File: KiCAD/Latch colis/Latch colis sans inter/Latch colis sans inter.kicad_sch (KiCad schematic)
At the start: 12 parts, among them J1 KF301-2P, J2 KF301-2P, J3 KF301-2P, J4 Jauges, K1 Relay_SPDT, K2 Relay_SPDT, Q1 2N2222A, U1 Heltec_LoRa32_V2_RST_side, U2 Module HX711

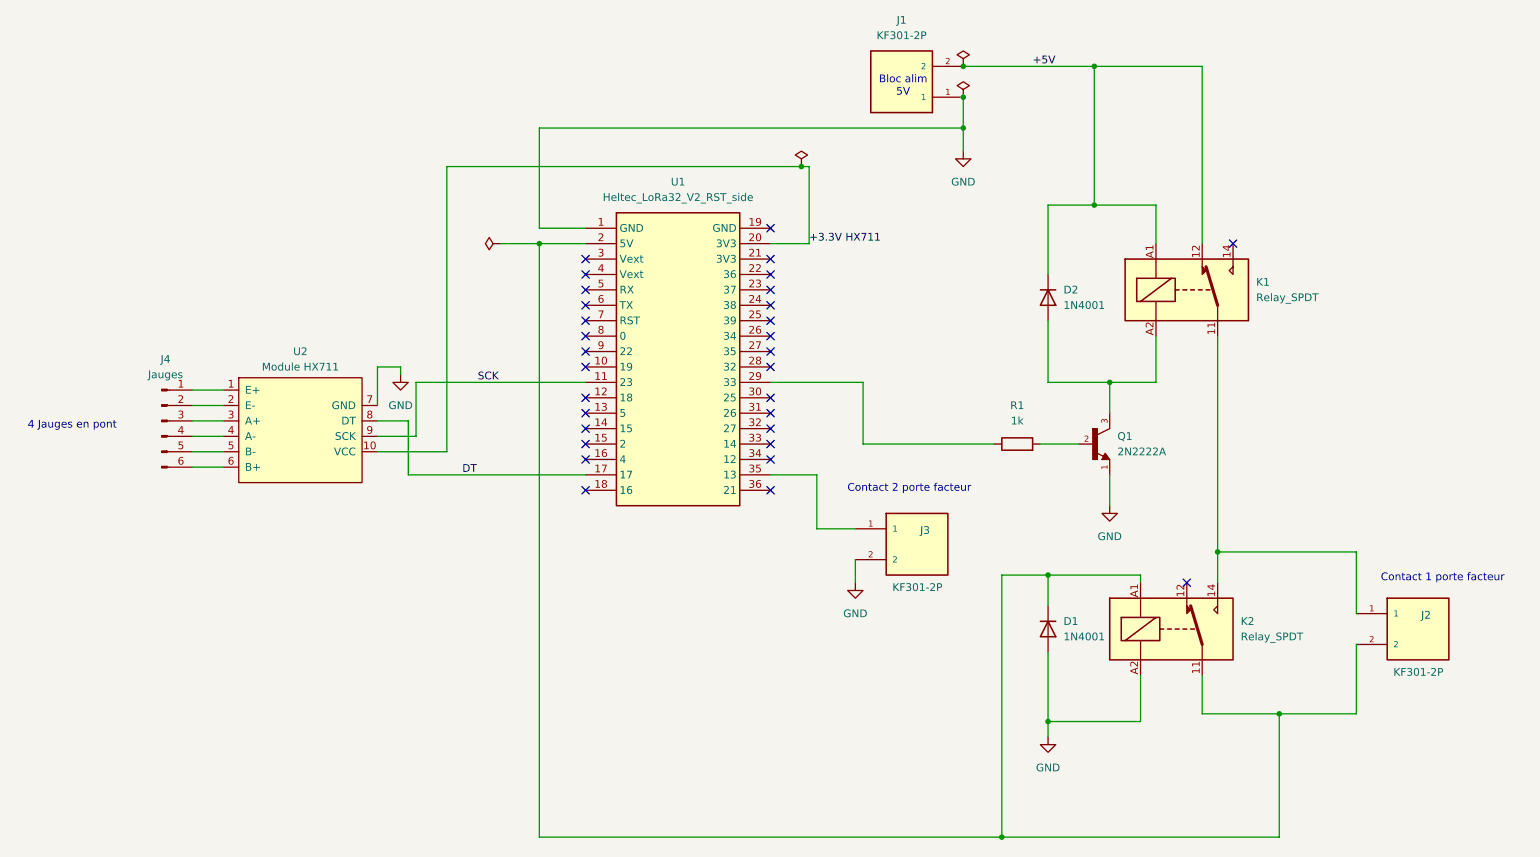
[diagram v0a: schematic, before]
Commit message: Passage au reveil par minuterie RTC, bibliotheques KiCad partagees, outils MCP
- Firmware courrier_emetteur : reveil profond par minuterie RTC au lieu du
  contact de porte, tarage HX711 persistant en memoire RTC, notification
  sans distinction nouveau/ancien courrier
- Variante "Latch colis sans inter" du schema KiCad, empreintes partagees
  (fp-lib-table) et PDF de brochage Heltec ajoutes
- Registre de travail (TODO.md) et espace de travail VS Code multi-dossiers
- Mise en place des serveurs MCP (Context7, Firecrawl, KiCad) avec script
  d'installation reutilisable sur une nouvelle machine (MCP-SETUP.md,
  setup-mcp-tools.ps1)

Co-Authored-By: Claude Sonnet 5 <noreply@anthropic.com>
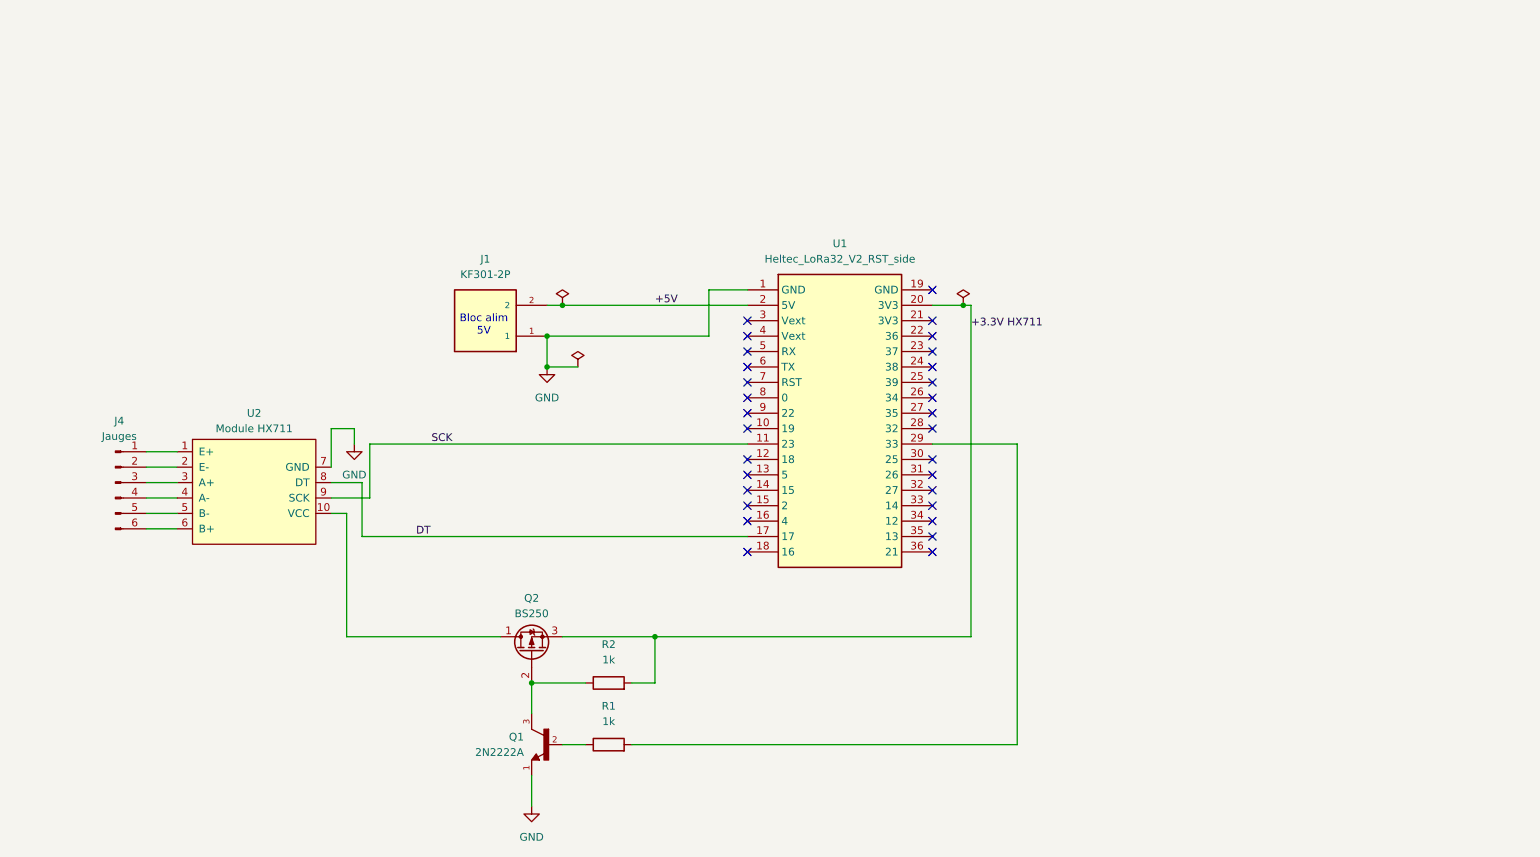
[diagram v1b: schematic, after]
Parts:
- removed D1, D2: 1N4001, Diode_THT:D_DO-41_SOD81_P10.16mm_Horizontal, symbol Ma bibliothèque:1N4001
- removed J2, J3: KF301-2P, Mes empreintes:KF301-2P, symbol Ma bibliothèque:KF301-2P
- removed K1, K2: Relay_SPDT, Mes empreintes:Relay_SPDT_SANYOU_SRD_Series_Form_C, symbol Ma bibliothèque:Relay_SPDT
- added Q2: BS250, Package_TO_SOT_THT:TO-92_Inline_Wide, symbol Transistor_FET:BS250
- added R2: 1k, Resistor_THT:R_Axial_DIN0207_L6.3mm_D2.5mm_P10.16mm_Horizontal, symbol Ma bibliothèque:R
- Q1: footprint Package_TO_SOT_THT:TO-92L_Inline_Wide -> Package_TO_SOT_THT:TO-92_Wide
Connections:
- net +3.3V HX711: now also Q2.3 (S), R2.2; no longer U2.10 (VCC)
- net +5V: now also U1.2 (5V)
- net at R1.1: now also Q1.2; no longer U1.29 (33)
- net at Q1.3: now also Q2.2 (G), R2.1
- net at R1.2: now also U1.29 (33); no longer Q1.2
- new net: Q2.1 (D), U2.10 (VCC)
- no-connect marks 31 -> 30
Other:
- note removed: "4 Jauges en pont"
- note removed: "Contact 1 porte facteur"
- note removed: "Contact 2 porte facteur"
- title: Gestion courrier boîtes aux lettres -> (none)

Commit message: Nettoyage ERC (no_connect) et reduction connecteur J4 a 4 broches
Suite a l'abandon des contacts de porte (design "sans inter"), les 2
signaux en trop du connecteur J4 n'ont plus lieu d'etre.

Co-Authored-By: Claude Sonnet 5 <noreply@anthropic.com>
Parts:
- J4: footprint Connector_PinHeader_2.54mm:PinHeader_1x06_P2.54mm_Vertical -> Connector_PinHeader_2.54mm:PinHeader_1x04_P2.54mm_Vertical
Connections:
- no-connect marks 30 -> 33
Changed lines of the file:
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@@
+	)
+	(no_connect
+		(at 29.21 104.14)
 	)
 	(no_connect
@@
 	)
 	(no_connect
+		(at 29.21 106.68)
+	)
+	(no_connect
 		(at 163.83 85.09)
+	)
+	(no_connect
+		(at 27.94 113.03)
 	)
 	(no_connect
@@
 			)
 		)
-		(property "Footprint" "Connector_PinHeader_2.54mm:PinHeader_1x06_P2.54mm_Vertical"
+		(property "Footprint" "Connector_PinHeader_2.54mm:PinHeader_1x04_P2.54mm_Vertical"
 			(at 29.21 99.06 0)
 			(hide yes)
